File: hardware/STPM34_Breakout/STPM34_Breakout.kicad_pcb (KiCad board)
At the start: 2 copper layers, 55 x 40 mm, 5 parts, among them U1 STPM34

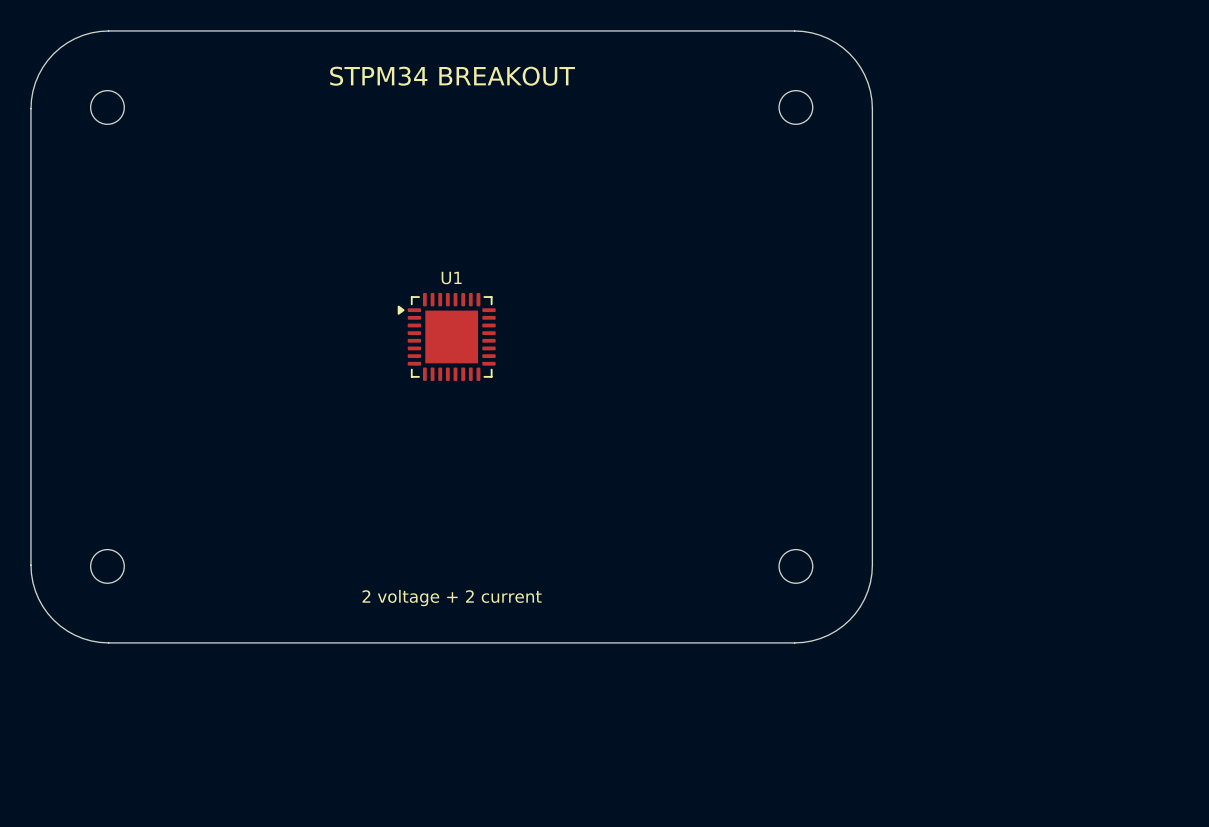
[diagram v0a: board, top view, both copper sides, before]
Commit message: Build production STPM34 breakout
Implement the dual-voltage dual-current schematic, routed PCB, sourcing metadata, project-local assets, renders, and ERC/DRC-gated Elecrow fabrication package.

Co-authored-by: Copilot <223556219+Copilot@users.noreply.github.com>
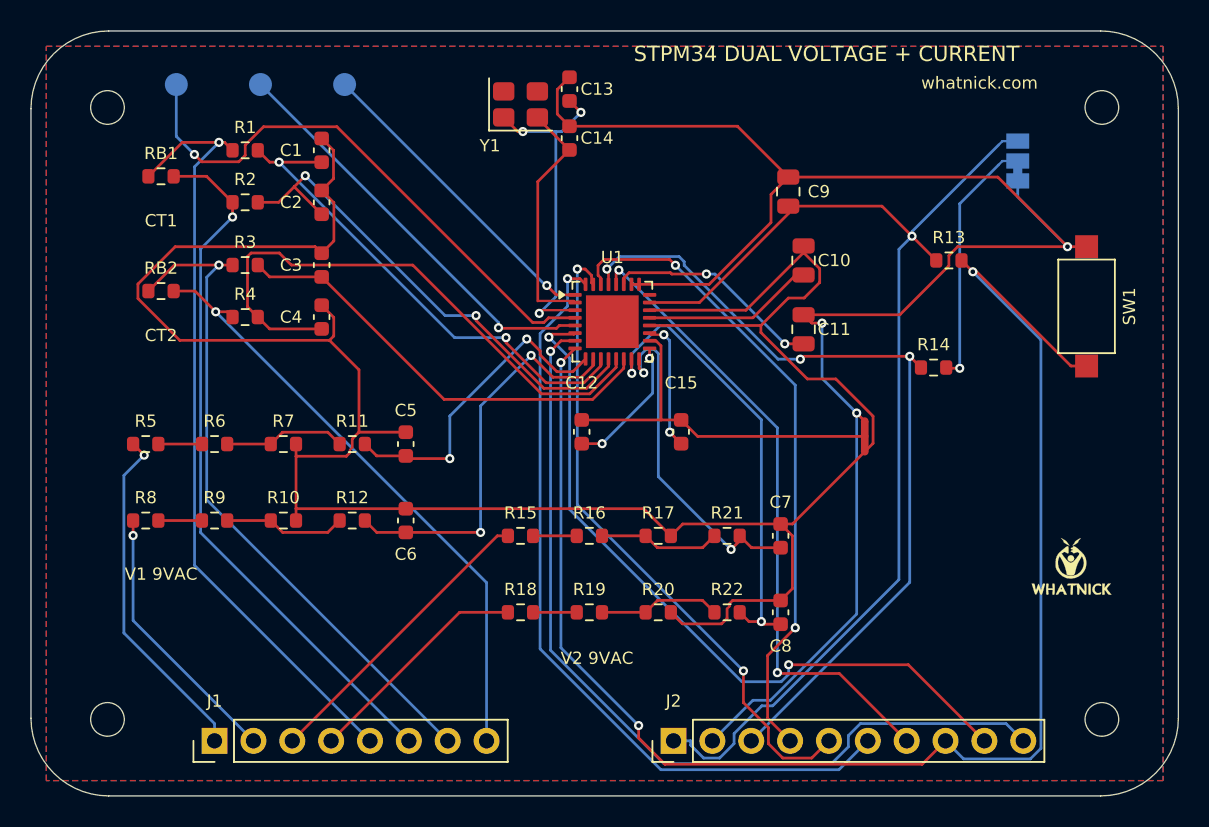
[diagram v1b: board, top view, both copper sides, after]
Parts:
- added C1: 330n, C_0603_1608Metric, F.Cu at (39.0, 27.8)
- added C10: 1u, C_0805_2012Metric, F.Cu at (70.5, 35.0)
- added C11: 4.7u, C_0805_2012Metric, F.Cu at (70.5, 39.5)
- added C12: 100n, C_0603_1608Metric, F.Cu at (56.0, 46.2)
- added C13: 15p, C_0603_1608Metric, F.Cu at (55.2, 23.8)
- added C14: 15p, C_0603_1608Metric, F.Cu at (55.2, 27.0)
- added C15: 100n, C_0603_1608Metric, F.Cu at (62.5, 46.2)
- added C2: 330n, C_0603_1608Metric, F.Cu at (39.0, 31.2)
- added C3: 330n, C_0603_1608Metric, F.Cu at (39.0, 35.3)
- added C4: 330n, C_0603_1608Metric, F.Cu at (39.0, 38.7)
- added C5: 33n, C_0603_1608Metric, F.Cu at (44.5, 47.0)
- added C6: 33n, C_0603_1608Metric, F.Cu at (44.5, 52.0)
- added C7: 33n, C_0603_1608Metric, F.Cu at (69.0, 53.0)
- added C8: 33n, C_0603_1608Metric, F.Cu at (69.0, 58.0)
- added C9: 1u, C_0805_2012Metric, F.Cu at (69.5, 30.5)
- added J1: ANALOG I/O, PinHeader_1x08_P2.54mm_Vertical, F.Cu at (32.0, 66.4)
- added J2: HOST I/O, PinHeader_1x10_P2.54mm_Vertical, F.Cu at (62.0, 66.4)
- added LOGO_OSHW: OSHW_Logo, OSHW_Logo, B.Cu at (88.0, 59.0)
- added LOGO_W: Whatnick_Logo, Whatnick_Logo, F.Cu at (88.0, 55.0)
- added NT1: ANALOG/DIGITAL STAR, NetTie-3_SMD_Pad0.5mm, F.Cu at (74.5, 46.5)
- added R1: 100R, R_0603_1608Metric, F.Cu at (34.0, 27.8)
- added R10: 2.49k, R_0603_1608Metric, F.Cu at (36.5, 52.0)
- added R11: 1k, R_0603_1608Metric, F.Cu at (41.0, 47.0)
- added R12: 1k, R_0603_1608Metric, F.Cu at (41.0, 52.0)
- added R13: 10k, R_0603_1608Metric, F.Cu at (80.0, 35.0)
- added R14: 10k, R_0603_1608Metric, F.Cu at (79.0, 42.0)
- added R15: 100k, R_0603_1608Metric, F.Cu at (52.0, 53.0)
- added R16: 100k, R_0603_1608Metric, F.Cu at (56.5, 53.0)
- added R17: 2.49k, R_0603_1608Metric, F.Cu at (61.0, 53.0)
- added R18: 100k, R_0603_1608Metric, F.Cu at (52.0, 58.0)
- added R19: 100k, R_0603_1608Metric, F.Cu at (56.5, 58.0)
- added R2: 100R, R_0603_1608Metric, F.Cu at (34.0, 31.2)
- added R20: 2.49k, R_0603_1608Metric, F.Cu at (61.0, 58.0)
- added R21: 1k, R_0603_1608Metric, F.Cu at (65.5, 53.0)
- added R22: 1k, R_0603_1608Metric, F.Cu at (65.5, 58.0)
- added R3: 100R, R_0603_1608Metric, F.Cu at (34.0, 35.3)
- added R4: 100R, R_0603_1608Metric, F.Cu at (34.0, 38.7)
- added R5: 100k, R_0603_1608Metric, F.Cu at (27.5, 47.0)
- added R6: 100k, R_0603_1608Metric, F.Cu at (32.0, 47.0)
- added R7: 2.49k, R_0603_1608Metric, F.Cu at (36.5, 47.0)
- added R8: 100k, R_0603_1608Metric, F.Cu at (27.5, 52.0)
- added R9: 100k, R_0603_1608Metric, F.Cu at (32.0, 52.0)
- added RB1: 2.4R, R_0603_1608Metric, F.Cu at (28.5, 29.5)
- added RB2: 2.4R, R_0603_1608Metric, F.Cu at (28.5, 37.0)
- added SJ1: SPI / UART, SolderJumper-3_P1.3mm_Bridged12_Pad1.0x1.5mm, B.Cu at (84.5, 28.5)
- added SW1: RESET, SW_SPST_CK_RS282G05A3, F.Cu at (89.0, 38.0)
- added TP1: LED1, TestPoint_Pad_D1.5mm, B.Cu at (29.5, 23.5)
- added TP2: LED2, TestPoint_Pad_D1.5mm, B.Cu at (35.0, 23.5)
- added TP3: CLKOUT_ZCR, TestPoint_Pad_D1.5mm, B.Cu at (40.5, 23.5)
- added Y1: 16MHz, Crystal_SMD_3225-4Pin_3.2x2.5mm, F.Cu at (52.0, 24.8)
- H1, H2, H3, H4: value M2 -> MountingHole_2.2mm_M2
- moved H4 22.4 mm to (90.0, 65.0)
- moved H2 20.0 mm to (90.0, 25.0)
- moved U1 10.5 mm to (58.0, 39.0)
- moved H3 10.0 mm to (25.0, 65.0)
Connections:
- U1 pad 1: (no net) -> CLKOUT_ZCR
- U1 pad 10: (no net) -> VIN1
- U1 pad 11: (no net) -> IIP1
- U1 pad 12: (no net) -> IIN1
- U1 pad 13: (no net) -> IIN2
- U1 pad 14: (no net) -> IIP2
- U1 pad 15: (no net) -> VIN2
- U1 pad 16: (no net) -> VIP2
- U1 pad 17: (no net) -> VREF1
- U1 pad 18: (no net) -> GND_REF
- U1 pad 19: (no net) -> VREF2
- U1 pad 2: (no net) -> XTAL2
- U1 pad 20: (no net) -> GNDA
- U1 pad 21: (no net) -> VDDA
- U1 pad 22: (no net) -> GNDA
- U1 pad 23: (no net) -> +3V3
- U1 pad 24: (no net) -> unconnected-(U1-NC-Pad24)
- U1 pad 25: (no net) -> DGND
- U1 pad 26: (no net) -> DGND
- U1 pad 27: (no net) -> VDDD
- U1 pad 28: (no net) -> SYN
- U1 pad 29: (no net) -> SCS
- U1 pad 3: (no net) -> XTAL1
- U1 pad 30: (no net) -> SCL
- U1 pad 31: (no net) -> MOSI_RXD
- U1 pad 32: (no net) -> MISO_TXD
- U1 pad 4: (no net) -> LED1
- U1 pad 5: (no net) -> LED2
- U1 pad 6: (no net) -> INT1
- U1 pad 7: (no net) -> INT2
- U1 pad 8: (no net) -> EN
- U1 pad 9: (no net) -> VIP1
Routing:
- net GNDA: track 0.00 -> 153.2 mm
- net DGND: track 0.00 -> 115.3 mm, vias 0 -> 3
- net EN: track 0.00 -> 100.4 mm, vias 0 -> 3
- net +3V3: track 0.00 -> 76.2 mm, vias 0 -> 1
- net INT2: track 0.00 -> 57.4 mm, vias 0 -> 1
- net SCS: track 0.00 -> 54.6 mm, vias 0 -> 3
- net MISO_TXD: track 0.00 -> 51.7 mm, vias 0 -> 1
- net CT1_P: track 0.00 -> 51.2 mm, vias 0 -> 1
- net INT1: track 0.00 -> 48.3 mm, vias 0 -> 2
- net CT1_N: track 0.00 -> 46.3 mm, vias 0 -> 1
- net CT2_P: track 0.00 -> 44.2 mm, vias 0 -> 1
- net MOSI_RXD: track 0.00 -> 42.7 mm, vias 0 -> 2
- net SCL: track 0.00 -> 42.4 mm, vias 0 -> 2
- net SYN: track 0.00 -> 41.9 mm, vias 0 -> 2
- net CT2_N: track 0.00 -> 39.9 mm, vias 0 -> 1
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- added copper zone on B.Cu, net DGND
- added copper zone on F.Cu, net GNDA
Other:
- board size 55 x 40 mm -> 75 x 50 mm
- board text added: "3V3"
- board text added: "CLK/ZCR"
- board text added: "CT1"
- board text added: "CT1+"
- board text added: "CT1-"
- board text added: "CT2"
- board text added: "CT2+"
- board text added: "CT2-"
- board text added: "EN"
- board text added: "GND"
- board text added: "INT1"
- board text added: "INT2"
- board text added: "ISOLATED 9VAC + CT INPUTS ONLY"
- board text added: "LED1"
- board text added: "LED2"
- board text added: "MISO"
- board text added: "MOSI"
- board text added: "NOT FOR DIRECT MAINS"
- board text added: "SCL"
- board text added: "SCS"
- board text added: "SPI"
- board text added: "STPM34 DUAL VOLTAGE + CURRENT"
- board text added: "SYN"
- board text added: "TAPR OHL 1.0"
- board text added: "UART"
- board text added: "V1 9VAC"
- board text added: "V1+"
- board text added: "V1-"
- board text added: "V2 9VAC"
- board text added: "V2+"
- board text added: "V2-"
- board text added: "v1.0 2026-10-10"
- board text added: "whatnick.com"
- board text removed: "2 voltage + 2 current"
- board text removed: "ANALOG INPUT / FILTER ZONE"
- board text removed: "POWER / DIGITAL I/O ZONE"
- board text removed: "STPM34 BREAKOUT"
- board text removed: "whatnick.com | TAPR OHL | NOT ISOLATED"
